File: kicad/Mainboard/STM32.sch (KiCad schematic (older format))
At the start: 37 parts, among them J11 VIB2, J3 USB_OTG, J4 SWD, J9 VIB1, Q1 BSS138, Q6 BSS138, U1 STM32F777VIT, U2 USBLC6-2SC6

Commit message: Mainboard: List of components -> Added TempCoef types, voltage values and tolerance for capaciors; added power values and tolerance for resistors
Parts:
- C1, C2, C20, C3, C4, C5: TempCoef (none) -> X7R; Voltage 25 -> 50
- C6, C7: TempCoef (none) -> C0G; Tolerance 2 -> 5; Voltage 25 -> 50
- R1, R2, R3, R4, R5, R67: Power (none) -> 0.125; Tolerance (none) -> 5
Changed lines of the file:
@@
 F 2 "Capacitor_SMD:C_0603_1608Metric" H 1400 1750 50  0001 C CNN
 F 3 "~" H 1400 1750 50  0001 C CNN
-F 4 "25" V 1400 1750 50  0001 C CNN "Voltage"
+F 4 "50" V 1400 1750 50  0001 C CNN "Voltage"
 F 5 "10" V 1400 1750 50  0001 C CNN "Tolerance"
+F 6 "X7R" H 1400 1750 50  0001 C CNN "TempCoef"
 	1    1400 1750
 	1    0    0    -1
@@
 F 2 "Capacitor_SMD:C_0603_1608Metric" H 1800 1750 50  0001 C CNN
 F 3 "~" H 1800 1750 50  0001 C CNN
-F 4 "25" H 1800 1750 50  0001 C CNN "Voltage"
+F 4 "50" H 1800 1750 50  0001 C CNN "Voltage"
 F 5 "10" H 1800 1750 50  0001 C CNN "Tolerance"
+F 6 "X7R" H 1800 1750 50  0001 C CNN "TempCoef"
 	1    1800 1750
 	1    0    0    -1
@@
 F 3 "~" H 6000 6050 50  0001 C CNN
 F 4 "10" H 6000 6050 50  0001 C CNN "Tolerance"
-F 5 "25" H 6000 6050 50  0001 C CNN "Voltage"
+F 5 "50" H 6000 6050 50  0001 C CNN "Voltage"
+F 6 "X7R" H 6000 6050 50  0001 C CNN "TempCoef"
 	1    6000 6050
 	1    0    0    1
@@
 F 3 "~" H 7750 2650 50  0001 C CNN
 F 4 "10" H 7750 2650 50  0001 C CNN "Tolerance"
-F 5 "25" H 7750 2650 50  0001 C CNN "Voltage"
+F 5 "50" H 7750 2650 50  0001 C CNN "Voltage"
+F 6 "X7R" H 7750 2650 50  0001 C CNN "TempCoef"
 	1    7750 2650
 	-1   0    0    1
@@
 F 2 "Resistor_SMD:R_0603_1608Metric" H 10150 3250 50  0001 C CNN
 F 3 "~" H 10150 3250 50  0001 C CNN
+F 4 "0.125" H 10150 3250 50  0001 C CNN "Power"
+F 5 "5" H 10150 3250 50  0001 C CNN "Tolerance"
 	1    10150 3250
 	1    0    0    -1
@@
 F 2 "Resistor_SMD:R_0603_1608Metric" H 8800 4900 50  0001 C CNN
 F 3 "~" H 8800 4900 50  0001 C CNN
+F 4 "0.125" H 8800 4900 50  0001 C CNN "Power"
+F 5 "5" H 8800 4900 50  0001 C CNN "Tolerance"
 	1    8800 4900
 	1    0    0    -1
@@
 F 2 "Capacitor_SMD:C_0603_1608Metric" H 8550 5700 50  0001 C CNN
 F 3 "~" H 8550 5700 50  0001 C CNN
-F 4 "25" V 8550 5700 50  0001 C CNN "Voltage"
+F 4 "50" V 8550 5700 50  0001 C CNN "Voltage"
 F 5 "10" H 8550 5700 50  0001 C CNN "Tolerance"
+F 6 "X7R" H 8550 5700 50  0001 C CNN "TempCoef"
 	1    8550 5700
 	1    0    0    1
@@
 F 2 "Capacitor_SMD:C_0603_1608Metric" H 10150 5900 50  0001 C CNN
 F 3 "~" H 10150 5900 50  0001 C CNN
-F 4 "2" H 10150 5900 50  0001 C CNN "Tolerance"
-F 5 "25" H 10150 5900 50  0001 C CNN "Voltage"
+F 4 "5" H 10150 5900 50  0001 C CNN "Tolerance"
+F 5 "50" H 10150 5900 50  0001 C CNN "Voltage"
+F 6 "C0G" H 10150 5900 50  0001 C CNN "TempCoef"
 	1    10150 5900
 	1    0    0    1
@@
 F 2 "Capacitor_SMD:C_0603_1608Metric" H 10350 5900 50  0001 C CNN
 F 3 "~" H 10350 5900 50  0001 C CNN
-F 4 "2" H 10350 5900 50  0001 C CNN "Tolerance"
-F 5 "25" H 10350 5900 50  0001 C CNN "Voltage"
+F 4 "5" H 10350 5900 50  0001 C CNN "Tolerance"
+F 5 "50" H 10350 5900 50  0001 C CNN "Voltage"
+F 6 "C0G" H 10350 5900 50  0001 C CNN "TempCoef"
 	1    10350 5900
 	-1   0    0    1
@@
 F 2 "Resistor_SMD:R_0603_1608Metric" H 10550 5300 50  0001 C CNN
 F 3 "~" H 10550 5300 50  0001 C CNN
+F 4 "0.125" H 10550 5300 50  0001 C CNN "Power"
+F 5 "5" H 10550 5300 50  0001 C CNN "Tolerance"
 	1    10550 5300
 	0    1    1    0
@@
 F 2 "Resistor_SMD:R_0603_1608Metric" H 10550 5700 50  0001 C CNN
 F 3 "~" H 10550 5700 50  0001 C CNN
+F 4 "0.125" H 10550 5700 50  0001 C CNN "Power"
+F 5 "5" H 10550 5700 50  0001 C CNN "Tolerance"
 	1    10550 5700
 	0    1    1    0
@@
 F 2 "Resistor_SMD:R_0603_1608Metric" H 9950 1250 50  0001 C CNN
 F 3 "~" H 9950 1250 50  0001 C CNN
+F 4 "0.125" H 9950 1250 50  0001 C CNN "Power"
+F 5 "5" H 9950 1250 50  0001 C CNN "Tolerance"
 	1    9950 1250
 	1    0    0    1
@@
 F 2 "Resistor_SMD:R_0603_1608Metric" H 8150 1950 50  0001 C CNN
 F 3 "~" H 8150 1950 50  0001 C CNN
+F 4 "0.125" H 8150 1950 50  0001 C CNN "Power"
+F 5 "5" H 8150 1950 50  0001 C CNN "Tolerance"
 	1    8150 1950
 	1    0    0    -1
@@
 F 3 "~" H 950 3350 50  0001 C CNN
 F 4 "10" H 950 3350 50  0001 C CNN "Tolerance"
-F 5 "25" H 950 3350 50  0001 C CNN "Voltage"
+F 5 "50" H 950 3350 50  0001 C CNN "Voltage"
+F 6 "X7R" H 950 3350 50  0001 C CNN "TempCoef"
 	1    950  3350
 	1    0    0    1

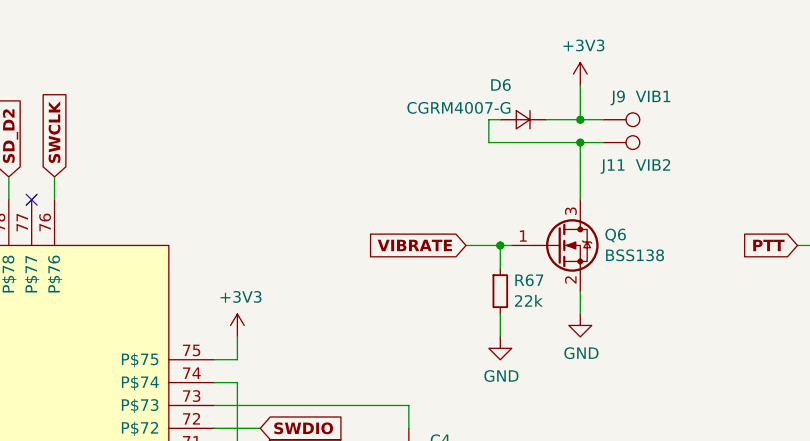
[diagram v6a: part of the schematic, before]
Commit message: Generated Gerbers for new HMI, corrected BOM for Mainboard
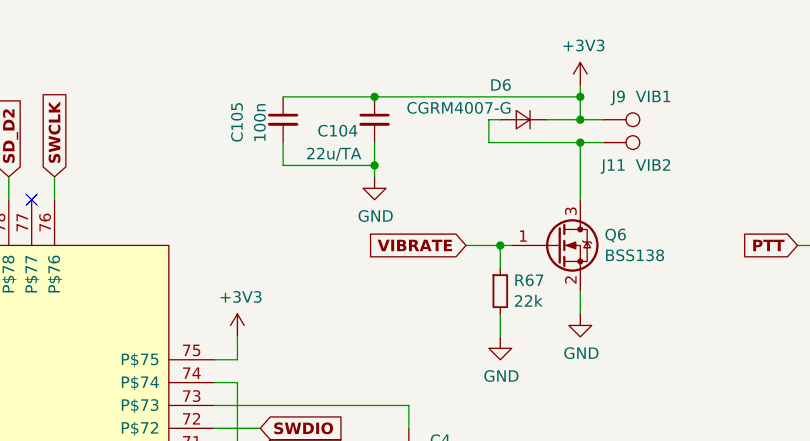
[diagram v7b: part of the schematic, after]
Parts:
- added C104: 22u/TA, Capacitor_Tantalum_SMD:CP_EIA-3216-18_Kemet-A, symbol Mainboard-rescue:C_Small-device
- added C105: 100n, Capacitor_SMD:C_0603_1608Metric, symbol Mainboard-rescue:C_Small-device
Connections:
- net +3V3: now also C104.1, C105.1
- net GND: now also C104.2, C105.2
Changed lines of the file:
@@
 	8600 1200 8500 1200
 Wire Wire Line
-	8500 1200 8500 1050
+	8500 1200 8500 1100
 Wire Wire Line
 	8500 1300 8500 1550
@@
 Wire Wire Line
 	2150 3150 2050 3150
+$Comp
+L Mainboard-rescue:C_Small-device C?
+U 1 1 5F24F494
+P 7600 1200
+AR Path="/5DEDCA32/5F24F494" Ref="C?"  Part="1"
+AR Path="/5DE274F4/5F24F494" Ref="C104"  Part="1"
+F 0 "C104" H 7350 1150 50  0000 L CNN
+F 1 "22u/TA" H 7300 1050 50  0000 L CNN
+F 2 "Capacitor_Tantalum_SMD:CP_EIA-3216-18_Kemet-A" H 7600 1200 50  0001 C CNN
+F 3 "~" H 7600 1200 50  0001 C CNN
+F 4 "TAJA226K006RNJV" H 7600 1200 50  0001 C CNN "Partno"
+F 5 "10" H 7600 1200 50  0001 C CNN "Tolerance"
+F 6 "10" H 7600 1200 50  0001 C CNN "Voltage"
+F 7 "TANTAL" H 7600 1200 50  0001 C CNN "TempCoef"
+	1    7600 1200
+	1    0    0    -1
+$EndComp
+Wire Wire Line
+	8500 1100 7600 1100
+Connection ~ 8500 1100
+Wire Wire Line
+	8500 1100 8500 1050
+$Comp
+L power:GND #PWR0174
+U 1 1 5F25F4B7
+P 7600 1450
+F 0 "#PWR0174" H 7600 1200 50  0001 C CNN
+F 1 "GND" H 7605 1277 50  0000 C CNN
+F 2 "" H 7600 1450 50  0001 C CNN
+F 3 "" H 7600 1450 50  0001 C CNN
+	1    7600 1450
+	1    0    0    -1
+$EndComp
+Wire Wire Line
+	7600 1300 7600 1400
+$Comp
+L Mainboard-rescue:C_Small-device C105
+U 1 1 5F26DD54
+P 7200 1200
+F 0 "C105" V 7000 1100 50  0000 L CNN
+F 1 "100n" V 7100 1100 50  0000 L CNN
+F 2 "Capacitor_SMD:C_0603_1608Metric" H 7200 1200 50  0001 C CNN
+F 3 "~" H 7200 1200 50  0001 C CNN
+F 4 "50" H 7200 1200 50  0001 C CNN "Voltage"
+F 5 "10" H 7200 1200 50  0001 C CNN "Tolerance"
+F 6 "X7R" H 7200 1200 50  0001 C CNN "TempCoef"
+	1    7200 1200
+	1    0    0    -1
+$EndComp
+Wire Wire Line
+	7600 1100 7200 1100
+Connection ~ 7600 1100
+Wire Wire Line
+	7200 1300 7200 1400
+Wire Wire Line
+	7200 1400 7600 1400
+Connection ~ 7600 1400
+Wire Wire Line
+	7600 1400 7600 1450
 $EndSCHEMATC

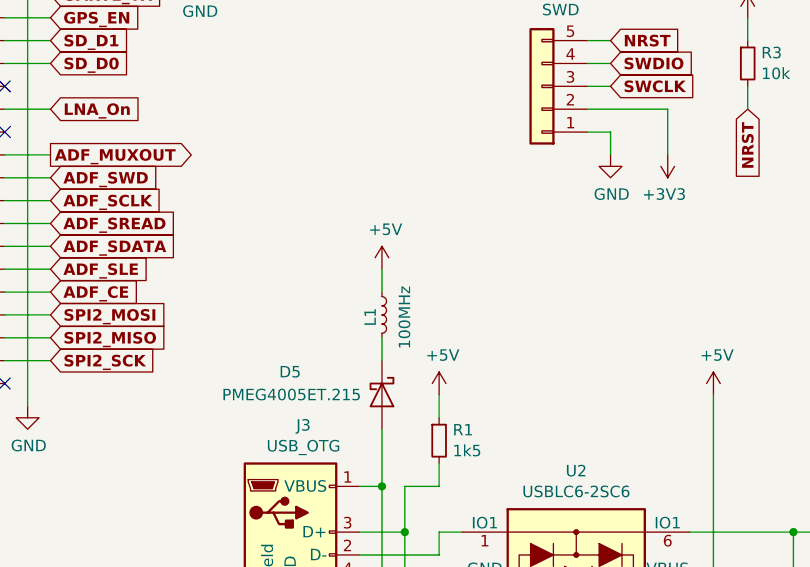
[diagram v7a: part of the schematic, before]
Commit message: Mainboard: corrected C47 & properly described C76, C79, C87 & assigned value to R20 & L1 is now Fair-Rite 2506032217Y2 & Volume pot is now Alps RK0971111Z32
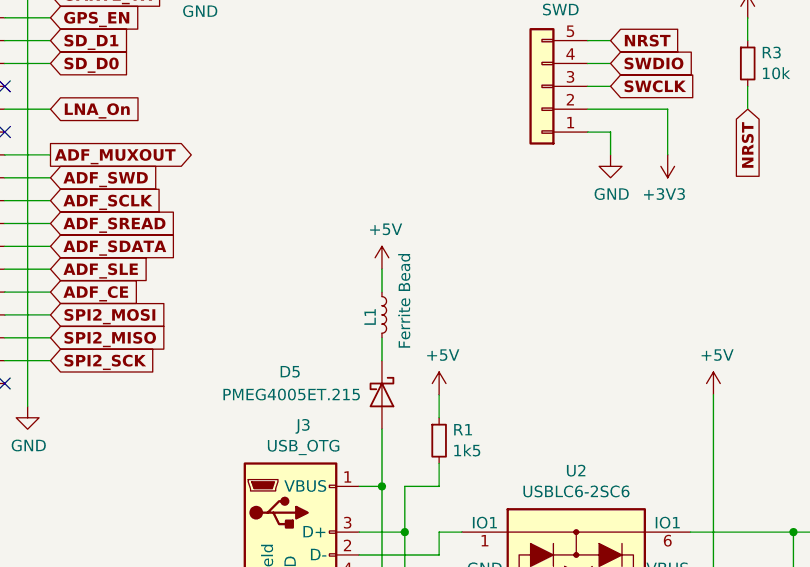
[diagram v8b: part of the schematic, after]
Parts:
- L1: value 100MHz -> Ferrite Bead; Partno (none) -> Fair-Rite 2506032217Y2
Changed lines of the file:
@@
 P 8550 4350
 F 0 "L1" V 8500 4300 50  0000 L CNN
-F 1 "100MHz" V 8650 4200 50  0000 L CNN
+F 1 "Ferrite Bead" V 8650 4200 50  0000 L CNN
 F 2 "Inductor_SMD:L_0603_1608Metric" H 8550 4350 50  0001 C CNN
 F 3 "~" H 8550 4350 50  0001 C CNN
+F 4 "Fair-Rite 2506032217Y2" H 8550 4350 50  0001 C CNN "Partno"
 	1    8550 4350
 	1    0    0    -1
